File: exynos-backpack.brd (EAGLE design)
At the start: 48 x 52 mm, 57 parts, among them IC1 MIC5335-SPYMT, IC2 TXS0108ERGY, IC3 LTC4352DD, IC4 LTC4352DD, IC5 LTC4352DD, J1 POWER_JACKPTH_LOCK, Q1 SI7234DP, Q2 SI7234DP, Q3 SI7234DP

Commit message: More work on backpack placement
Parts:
- removed C1, C2, C3, C4, C5, C6: 0.1uF, biomimetic:0402-CAP
- removed C7, C8, C9: 22uF, biomimetic:0603-CAP
- removed D1, D2, D3: PESD5V0S1UA, biomimetic:SOD-323
- removed IC3, IC4, IC5: LTC4352DD, biomimetic:DFN-12-3X3-DD
- removed J1: POWER_JACKPTH_LOCK, biomimetic:POWER_JACK_PTH_LOCK
- removed JP5, JP6: JST-RCY-MALE, biomimetic:JST-RCY-MALE
- removed LED1, LED3, LED5: FAULT_BATTA, biomimetic:LED-0603
- removed LED2, LED4, LED6: STATUS_BATTA, biomimetic:LED-0603
- removed Q1, Q2, Q3: SI7234DP, biomimetic:POWERPAK-SO-8-DUAL
- removed R1, R11: 1.5k, biomimetic:0402-RES
- removed R10, R9: 510, biomimetic:0402-RES
- removed R12, R2: 20k, biomimetic:0402-RES
- removed R13, R3, R8: 2.7k, biomimetic:0402-RES
- removed R14, R15, R4, R5: 330, biomimetic:0402-RES
- removed R6: 910, biomimetic:0402-RES
- removed R7: 27k, biomimetic:0402-RES
- added JP3: JST-RCY-MALE, biomimetic:JST-RCY-MALE
- moved PS1 76.1 mm to (16.0, 25.0)
- moved C10 44.2 mm to (15.5, 38.4), turned to 180 degrees
- moved C11 38.5 mm to (15.5, 16.8)
- moved JP7 37.5 mm to (-23.8, 27.9), turned to 90 degrees
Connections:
- removed net N$1: C1.2, IC3.12, Q1.1, Q1.3
- removed net N$10: IC3.5, LED2.C
- removed net N$11: LED2.A, R5.1
- removed net N$12: LED1.A, R4.1
- removed net N$13: C3.2, IC5.12, Q2.1, Q2.3
- removed net N$14: IC5.11, Q2.2, Q2.4
- removed net N$15: C3.1, IC5.10
- removed net N$18: IC5.3, R6.2, R7.1
- removed net N$19: IC5.4, R6.1, R8.2
- removed net N$2: IC3.11, Q1.2, Q1.4
- removed net N$20: C4.1, IC5.2
- removed net N$21: IC5.6, LED3.C
- removed net N$22: IC5.5, LED4.C
- removed net N$23: LED4.A, R10.1
- removed net N$24: LED3.A, R9.1
- removed net N$25: C5.2, IC4.12, Q3.1, Q3.3
- removed net N$26: IC4.11, Q3.2, Q3.4
- removed net N$27: C5.1, IC4.10
- removed net N$30: IC4.3, R11.2, R12.1
- removed net N$31: IC4.4, R11.1, R13.2
- removed net N$32: C6.1, IC4.2
- removed net N$33: IC4.6, LED5.C
- removed net N$34: IC4.5, LED6.C
- removed net N$35: LED6.A, R15.1
- removed net N$36: LED5.A, R14.1
- removed net N$4: C1.1, IC3.10
- removed net N$6: IC3.3, R1.2, R2.1
- removed net N$7: IC3.4, R1.1, R3.2
- removed net N$8: C2.1, IC3.2
- removed net N$9: IC3.6, LED1.C
- removed net V_BATTA: C7.1, D1.1, IC3.1, Q1.7+8, R2.2, R4.2, R5.2
- removed net V_BATTB: C8.1, D2.1, IC4.1, Q3.7+8, R12.2, R14.2, R15.2
- removed net V_WALL: C9.1, D3.1, IC5.1, Q2.7+8, R10.2, R7.2, R9.2
- net GND: no longer C2.2, C4.2, C6.2, C7.2, C8.2, C9.2, D1.2, D2.2, D3.2, IC3.7, IC3.9, IC3.PAD, IC4.7, IC4.9, IC4.PAD, IC5.7, IC5.9, IC5.PAD, R13.1, R3.1, R8.1
- net V_OR: no longer IC3.8, IC4.8, IC5.8, Q1.5+6, Q2.5+6, Q3.5+6
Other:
- outline, holes or cut-outs redrawn

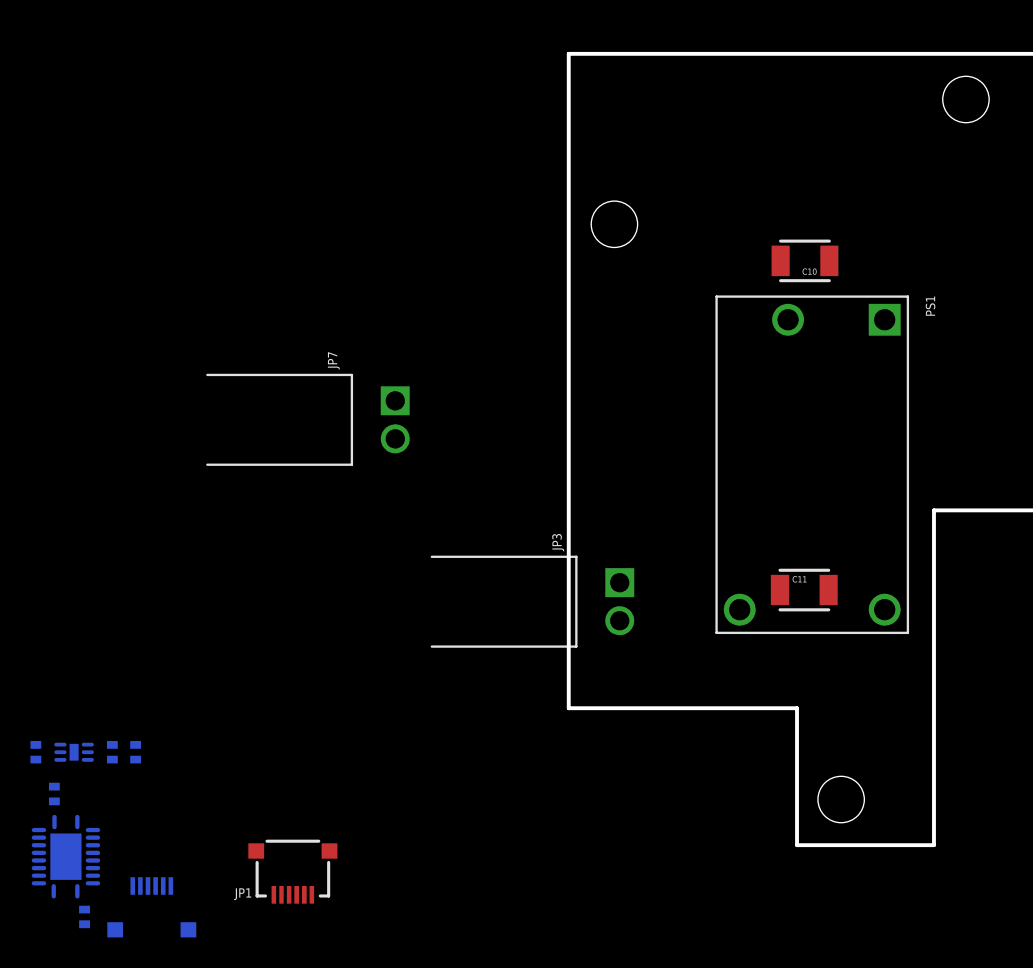
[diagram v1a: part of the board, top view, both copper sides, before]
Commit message: First pass at exynos backpack placement
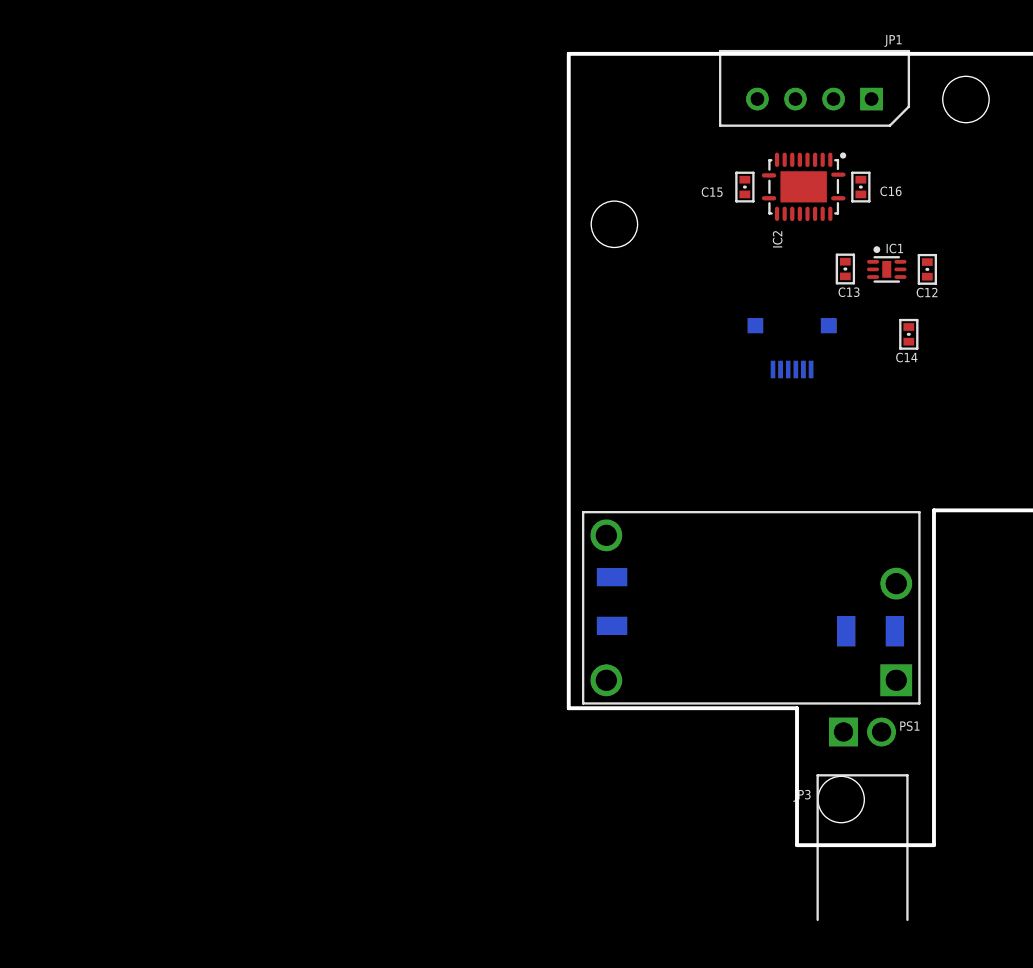
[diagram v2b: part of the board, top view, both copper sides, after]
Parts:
- removed JP7: JST-RCY-MALE, biomimetic:JST-RCY-MALE
- IC2: value TXS0108ERGY -> TXB0108RGY
- JP1: value CONSOLE -> (none); device biomimetic:MOLEX_503480-0600 -> biomimetic:1X04_MOLEX_5267
- moved C16 70.0 mm to (19.2, 43.2), flipped to the top, turned to 90 degrees
- moved C12 66.6 mm to (23.6, 37.8), flipped to the top, turned to 270 degrees
- moved IC2 65.5 mm to (15.4, 43.3), flipped to the top, turned to 180 degrees
- moved JP1 63.3 mm to (19.9, 49.0)
- moved IC1 62.1 mm to (20.9, 37.8), flipped to the top, turned to 270 degrees
- moved C15 60.4 mm to (11.6, 43.2), flipped to the top, turned to 270 degrees
- moved C14 59.1 mm to (22.3, 33.6), flipped to the top, turned to 270 degrees
- moved C13 56.4 mm to (18.2, 37.9), flipped to the top, turned to 270 degrees
- moved JP2 56.3 mm to (14.7, 33.0), turned to 180 degrees
- moved JP3 35.2 mm to (19.3, -4.91), turned to 180 degrees
- moved C10 24.7 mm to (19.8, 14.1), flipped to the bottom, turned to 0 degrees
- moved C11 12.7 mm to (2.84, 16.0), flipped to the bottom, turned to 270 degrees
- moved PS1 10.2 mm to (12.0, 15.6), turned to 180 degrees
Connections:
- removed net UART_RX_1V8: IC2.3, JP1.4
- removed net UART_RX_3V3: IC2.18, JP2.4
- removed net UART_TX_1V8: IC2.1, JP1.5
- removed net UART_TX_3V3: IC2.20, JP2.6
- removed net V_OR: C10.1, PS1.2
- new net IMAGEPROC_RXD: IC2.18
- new net IMAGEPROC_TXD: IC2.17
- new net ODROID_RXD: IC2.4, JP1.3
- new net ODROID_TXD: IC2.3, JP1.2
- net 1.8V: now also IC2.1, JP1.1
- net 3.3V: now also IC2.20
- net GND: now also IC2.12, IC2.13, IC2.14, IC2.15, IC2.16, IC2.5, IC2.6, IC2.7, IC2.8, IC2.9, JP1.4, JP3.1; no longer JP1.1, JP2.3, JP2.5
- net V_BATT: now also C10.1, JP3.2, PS1.2; no longer JP2.1, JP2.2

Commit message: Finish placement
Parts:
- added JP4: JST-RCY-FEMALE-NOSILK, biomimetic:JST-RCY-FEMALE_NOSILK
- added JP5: ODROID CONSOLE, biomimetic:1X04_MOLEX_5267
- JP1: value (none) -> ODROID
- JP3: value JST-RCY-MALE -> JST-RCY-MALE-NOSILK; device biomimetic:JST-RCY-MALE -> biomimetic:JST-RCY-MALE_NOSILK
- moved C12 15.3 mm to (16.5, 24.2), turned to 90 degrees
- moved C13 14.0 mm to (21.3, 24.2)
- moved IC1 13.8 mm to (18.9, 24.2)
- moved C14 9.35 mm to (22.9, 24.2)
- moved C15 7.21 mm to (18.7, 44.0), turned to 0 degrees
- moved C11 6.14 mm to (6.55, 11.1), turned to 180 degrees
- moved JP3 4.91 mm to (19.5, 0.00)
- moved C16 2.89 mm to (18.7, 40.4), turned to 0 degrees
- moved JP2 1.78 mm to (14.9, 34.7), flipped to the top, turned to 0 degrees
- moved IC2 1.32 mm to (14.6, 42.2)
- moved C10 0.17 mm to (20.0, 14.2)
- moved PS1 0.11 mm to (12.0, 15.7)
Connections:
- net 1.8V: now also JP5.1; no longer IC2.1
- net 3.3V: no longer IC2.20
- net 5V: now also JP4.2
- net GND: now also IC2.1, IC2.20, JP2.3, JP2.5, JP4.1, JP5.4
- net IMAGEPROC_RXD: now also JP2.6
- net IMAGEPROC_TXD: now also JP2.4
- net ODROID_RXD: now also JP5.3
- net ODROID_TXD: now also JP5.2
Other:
- board size 48 x 52 mm -> 29 x 52 mm
